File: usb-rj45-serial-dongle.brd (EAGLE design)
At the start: 33 x 17 mm, 16 parts, among them J1 RJHSE-5081, J2 USBPCB_NOPASTE, U1 CP2102N-A01-GQFN20R, U2 MAX202ECWE, U3 SP0503BAHTG

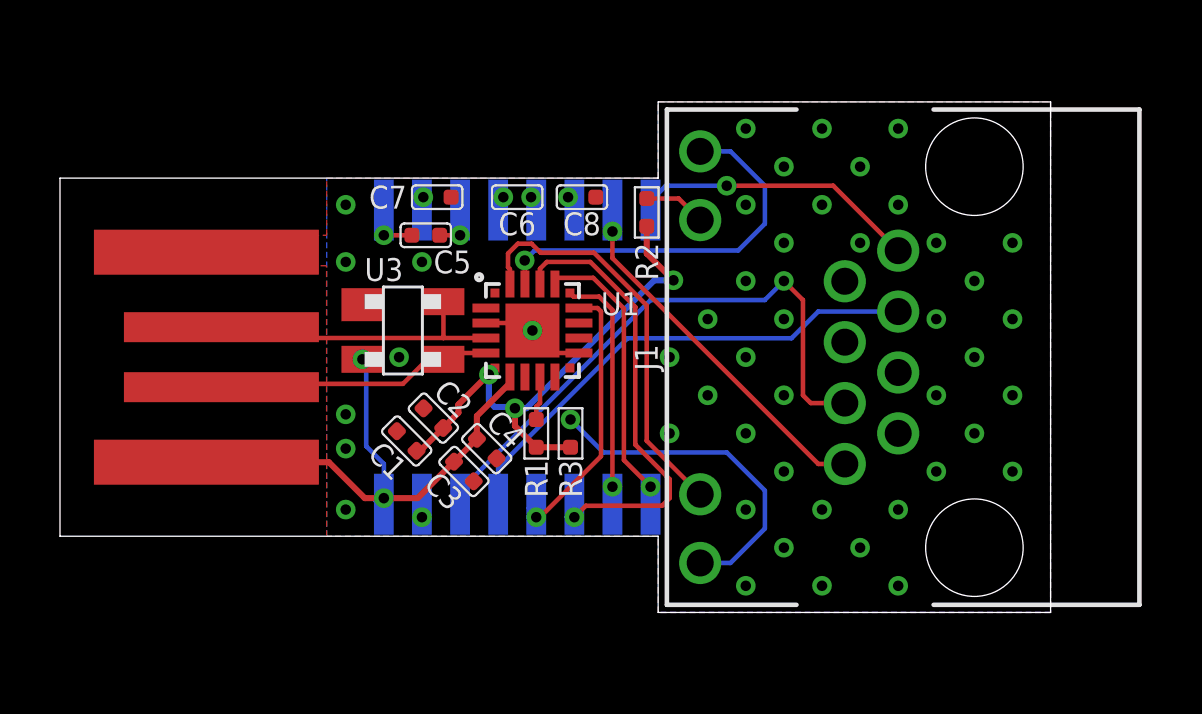
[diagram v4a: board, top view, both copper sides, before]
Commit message: Add VBUS voltage divider per CP2102N datasheet; Fix CTS/RXD swapped at MAX202E; Routing improvements
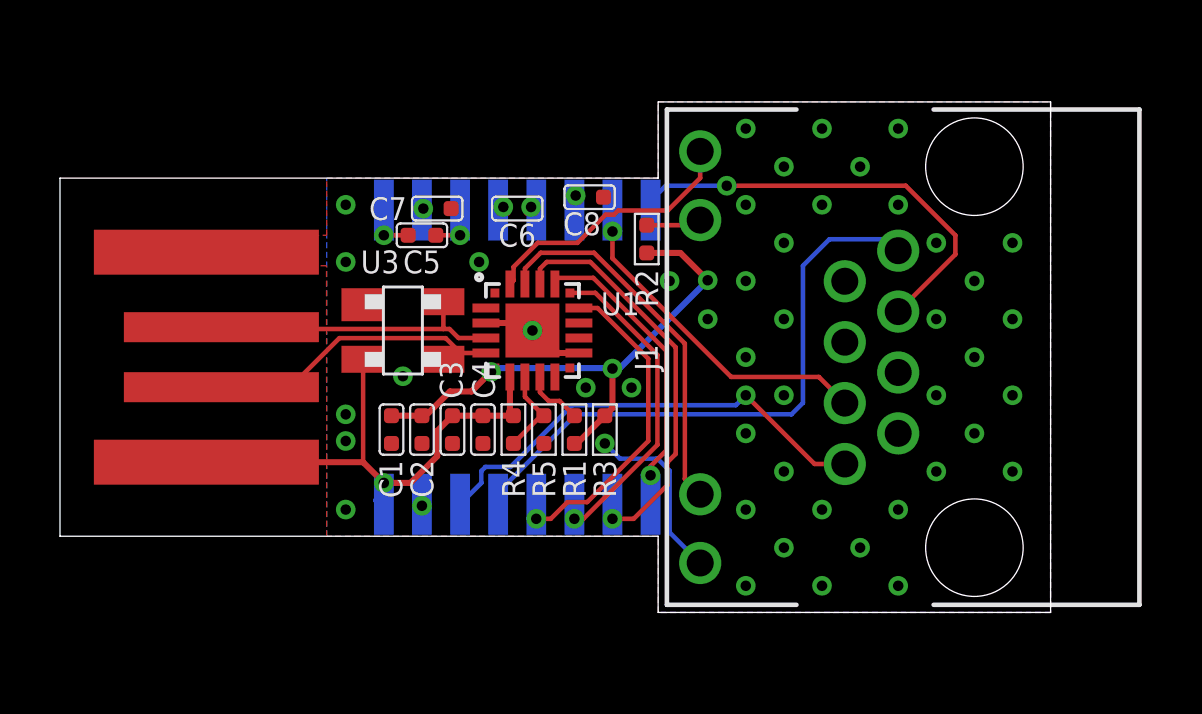
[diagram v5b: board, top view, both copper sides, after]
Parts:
- added R4: 22K, OPL_Resistor:R0402
- added R5: 47K, OPL_Resistor:R0402
- moved C3 1.45 mm to (13.1, 6.48), turned to 0 degrees
- moved R1 1.28 mm to (17.1, 6.48)
- moved R3 1.15 mm to (18.2, 6.48), turned to 0 degrees
- moved R2 0.89 mm to (19.6, 12.8)
- moved C4 0.65 mm to (14.1, 6.48), turned to 0 degrees
- moved C1 0.64 mm to (11.0, 6.48), turned to 0 degrees
- moved C2 0.54 mm to (12.1, 6.48), turned to 0 degrees
- moved C6 0.38 mm to (15.2, 13.8)
- moved C7 0.38 mm to (12.6, 13.8)
- moved C8 0.25 mm to (17.7, 14.2)
- moved C5 0.13 mm to (12.1, 13.0)
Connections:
- net CTS: now also U2.13; no longer U2.8
- net GND: now also R5.1
- net RTS: now also U2.14; no longer U2.7
- net RXD: now also U2.8; no longer U2.13
- net RXT_LED: now also J1.11; no longer J1.9
- net TXD: now also U2.7; no longer U2.14
- net TXT_LED: now also J1.9; no longer J1.11
- net UART_RTS: now also U2.11; no longer U2.10
- net UART_TXD: now also U2.10; no longer U2.11
- net VBUS: now also R4.1, R5.2
- net VCC: now also R4.2
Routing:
- net CTS: track 10.4 -> 20.5 mm, vias 1 -> 0
- net TXD: track 19.7 -> 11.4 mm
- net N$3: track 11.4 -> 6.03 mm
- net TXT_LED: track 13.7 -> 8.97 mm
- net RTS: track 12.2 -> 15.5 mm
- net VBUS: track 0.00 -> 2.95 mm
- net UART_RTS: track 8.13 -> 11.0 mm
- net UART_CTS: track 9.33 -> 11.0 mm
- net RXD: track 16.7 -> 15.1 mm, vias 0 -> 1
- net UART_TXD: track 15.1 -> 13.8 mm
- net USBDN: track 9.41 -> 10.6 mm
- net UART_RXD: track 9.82 -> 10.8 mm
- net RXT_LED: track 13.2 -> 12.6 mm, vias 1 -> 0
- net N$2: track 1.47 -> 1.98 mm
- net VCC: track 18.4 -> 17.9 mm, vias 2 -> 1
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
